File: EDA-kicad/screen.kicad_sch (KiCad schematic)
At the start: 3 parts

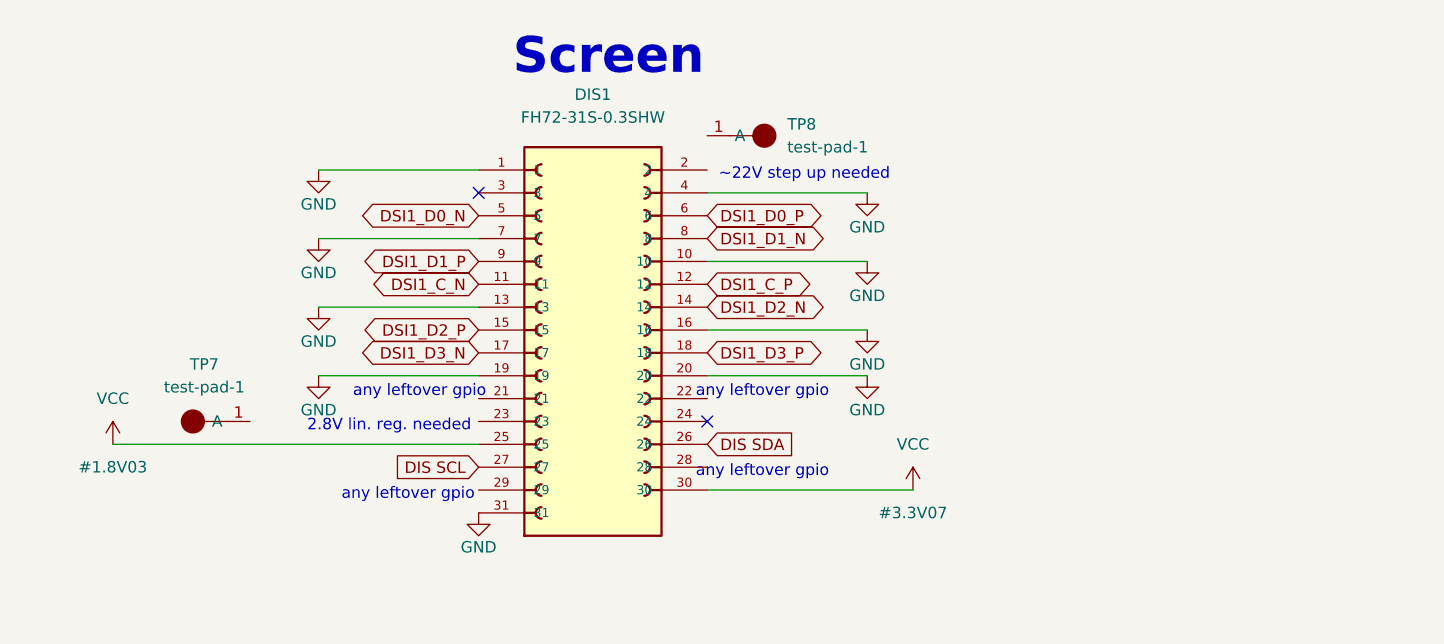
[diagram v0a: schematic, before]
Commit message: schematic cleaned up a bit
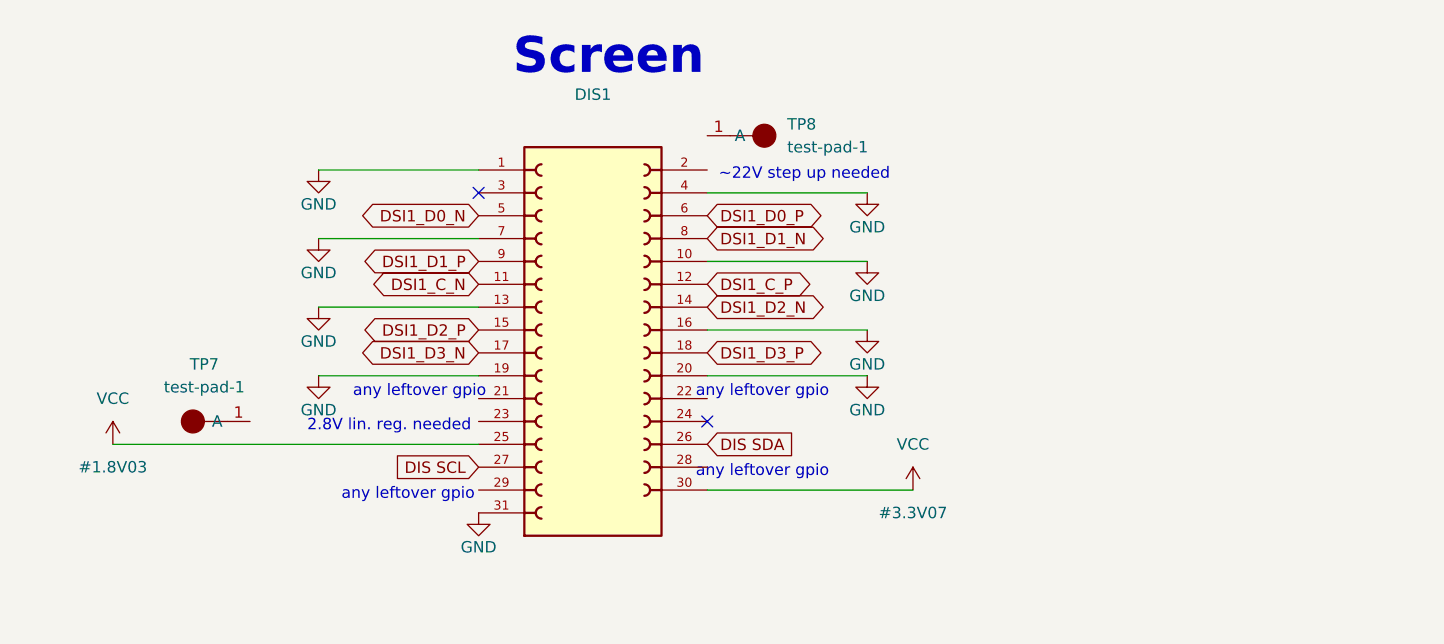
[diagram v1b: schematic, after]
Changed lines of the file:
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@@
 					(size 1.27 1.27)
 				)
+				(hide yes)
 			)
 		)
@@
 			)
 		)
-		(property "Description" "\n31 Position FPC Connector Contacts, Top 0.012 (0.30mm) Surface Mount, Right Angle\n"
+		(property "Description" "31 Position FPC Connector Contacts, Top 0.012 (0.30mm) Surface Mount, Right Angle"
 			(at 149.86 90.17 0)
 			(effects

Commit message: reannotate entire schematic
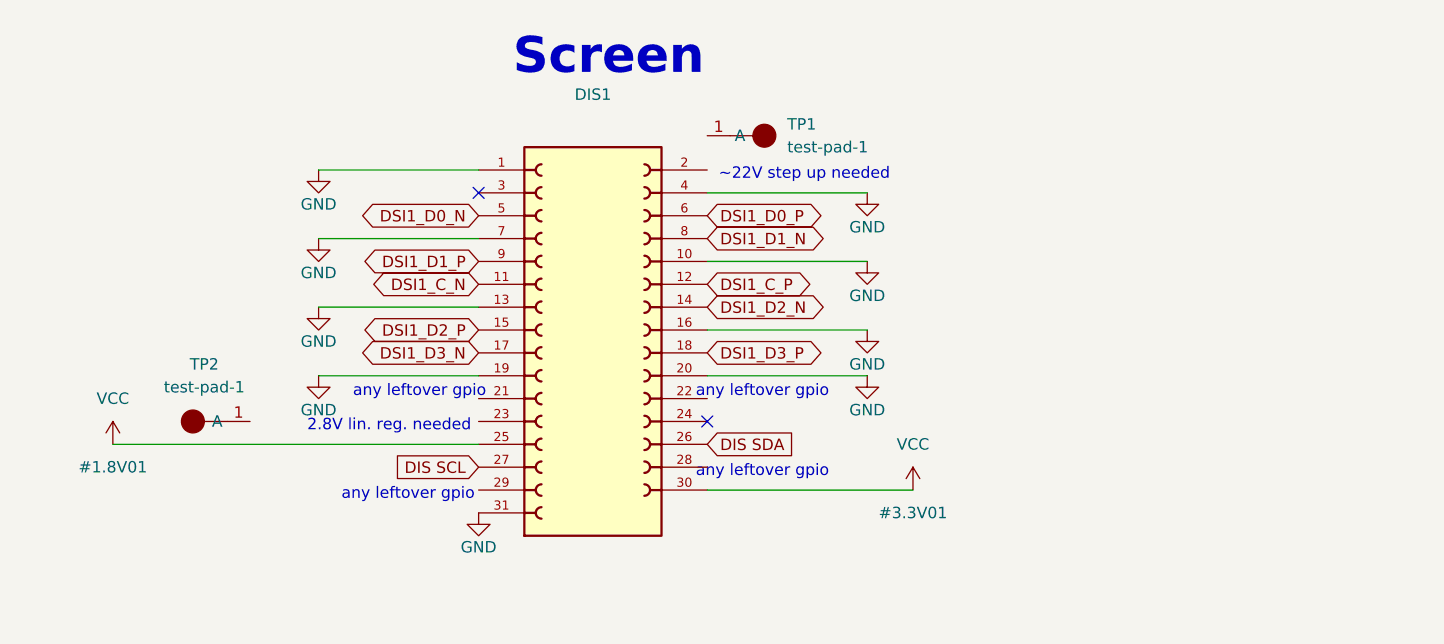
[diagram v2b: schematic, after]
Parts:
- renumbered TP8 to TP1, TP7 to TP2
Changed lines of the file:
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@@
 		(dnp no)
 		(fields_autoplaced yes)
-		(property "Reference" "TP7"
+		(property "Reference" "TP2"
 			(at 106.68 93.98 0)
 			(effects
@@
 			(project "cm5-carrier"
 				(path "/28c5e4fe-1ec7-4477-97f0-d2ec1401fad5/02797719-74e3-4dee-b809-c2968ee0cdff"
-					(reference "TP7")
+					(reference "TP2")
 					(unit 1)
 				)
@@
 		(on_board yes)
 		(dnp no)
-		(property "Reference" "#PWR070"
+		(property "Reference" "#PWR060"
 			(at 119.38 101.6 0)
 			(effects
@@
 			(project "cm5-carrier"
 				(path "/28c5e4fe-1ec7-4477-97f0-d2ec1401fad5/02797719-74e3-4dee-b809-c2968ee0cdff"
-					(reference "#PWR070")
+					(reference "#PWR060")
 					(unit 1)
 				)
@@
 		(on_board yes)
 		(dnp no)
-		(property "Reference" "#PWR067"
+		(property "Reference" "#PWR054"
 			(at 119.38 78.74 0)
 			(effects
@@
 			(project "cm5-carrier"
 				(path "/28c5e4fe-1ec7-4477-97f0-d2ec1401fad5/02797719-74e3-4dee-b809-c2968ee0cdff"
-					(reference "#PWR067")
+					(reference "#PWR054")
 					(unit 1)
 				)
@@
 		(on_board yes)
 		(dnp no)
-		(property "Reference" "#PWR074"
+		(property "Reference" "#PWR059"
 			(at 180.34 96.52 0)
 			(effects
@@
 			(project "cm5-carrier"
 				(path "/28c5e4fe-1ec7-4477-97f0-d2ec1401fad5/02797719-74e3-4dee-b809-c2968ee0cdff"
-					(reference "#PWR074")
+					(reference "#PWR059")
 					(unit 1)
 				)
@@
 		(on_board yes)
 		(dnp no)
-		(property "Reference" "#PWR075"
+		(property "Reference" "#PWR061"
 			(at 180.34 101.6 0)
 			(effects
@@
 			(project "cm5-carrier"
 				(path "/28c5e4fe-1ec7-4477-97f0-d2ec1401fad5/02797719-74e3-4dee-b809-c2968ee0cdff"
-					(reference "#PWR075")
+					(reference "#PWR061")
 					(unit 1)
 				)
@@
 		(on_board yes)
 		(dnp no)
-		(property "Reference" "#3.3V07"
+		(property "Reference" "#3.3V01"
 			(at 185.42 110.49 0)
 			(effects
@@
 			(project "cm5-carrier"
 				(path "/28c5e4fe-1ec7-4477-97f0-d2ec1401fad5/02797719-74e3-4dee-b809-c2968ee0cdff"
-					(reference "#3.3V07")
+					(reference "#3.3V01")
 					(unit 1)
 				)
@@
 		(dnp no)
 		(fields_autoplaced yes)
-		(property "Reference" "TP8"
+		(property "Reference" "TP1"
 			(at 171.45 67.3099 0)
 			(effects
@@
 			(project "cm5-carrier"
 				(path "/28c5e4fe-1ec7-4477-97f0-d2ec1401fad5/02797719-74e3-4dee-b809-c2968ee0cdff"
-					(reference "TP8")
+					(reference "TP1")
 					(unit 1)
 				)
@@
 		(on_board yes)
 		(dnp no)
-		(property "Reference" "#PWR069"
+		(property "Reference" "#PWR058"
 			(at 119.38 93.98 0)
 			(effects
@@
 			(project "cm5-carrier"
 				(path "/28c5e4fe-1ec7-4477-97f0-d2ec1401fad5/02797719-74e3-4dee-b809-c2968ee0cdff"
-					(reference "#PWR069")
+					(reference "#PWR058")
 					(unit 1)
 				)
@@
 		(on_board yes)
 		(dnp no)
-		(property "Reference" "#PWR071"
+		(property "Reference" "#PWR062"
 			(at 137.16 116.84 0)
 			(effects
@@
 			(project "cm5-carrier"
 				(path "/28c5e4fe-1ec7-4477-97f0-d2ec1401fad5/02797719-74e3-4dee-b809-c2968ee0cdff"
-					(reference "#PWR071")
+					(reference "#PWR062")
 					(unit 1)
 				)
@@
 		(on_board yes)
 		(dnp no)
-		(property "Reference" "#PWR068"
+		(property "Reference" "#PWR056"
 			(at 119.38 86.36 0)
 			(effects
@@
 			(project "cm5-carrier"
 				(path "/28c5e4fe-1ec7-4477-97f0-d2ec1401fad5/02797719-74e3-4dee-b809-c2968ee0cdff"
-					(reference "#PWR068")
+					(reference "#PWR056")
 					(unit 1)
 				)
@@
 		(on_board yes)
 		(dnp no)
-		(property "Reference" "#1.8V03"
+		(property "Reference" "#1.8V01"
 			(at 96.52 105.41 0)
 			(effects
@@
 			(project "cm5-carrier"
 				(path "/28c5e4fe-1ec7-4477-97f0-d2ec1401fad5/02797719-74e3-4dee-b809-c2968ee0cdff"
-					(reference "#1.8V03")
+					(reference "#1.8V01")
 					(unit 1)
 				)
@@
 		(on_board yes)
 		(dnp no)
-		(property "Reference" "#PWR072"
+		(property "Reference" "#PWR055"
 			(at 180.34 81.28 0)
 			(effects
@@
 			(project "cm5-carrier"
 				(path "/28c5e4fe-1ec7-4477-97f0-d2ec1401fad5/02797719-74e3-4dee-b809-c2968ee0cdff"
-					(reference "#PWR072")
+					(reference "#PWR055")
 					(unit 1)
 				)
@@
 		(on_board yes)
 		(dnp no)
-		(property "Reference" "#PWR073"
+		(property "Reference" "#PWR057"
 			(at 180.34 88.9 0)
 			(effects
@@
 			(project "cm5-carrier"
 				(path "/28c5e4fe-1ec7-4477-97f0-d2ec1401fad5/02797719-74e3-4dee-b809-c2968ee0cdff"
-					(reference "#PWR073")
-					(unit 1)
-				)
+					(reference "#PWR057")
+					(unit 1)
+				)

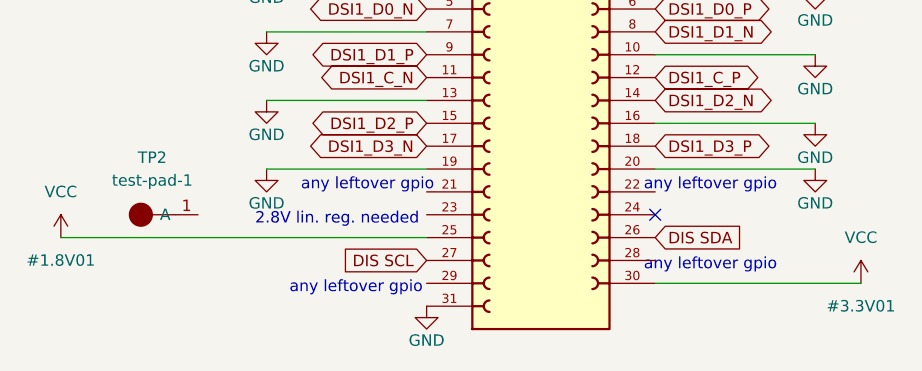
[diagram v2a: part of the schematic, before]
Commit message: add new switches and reannotate
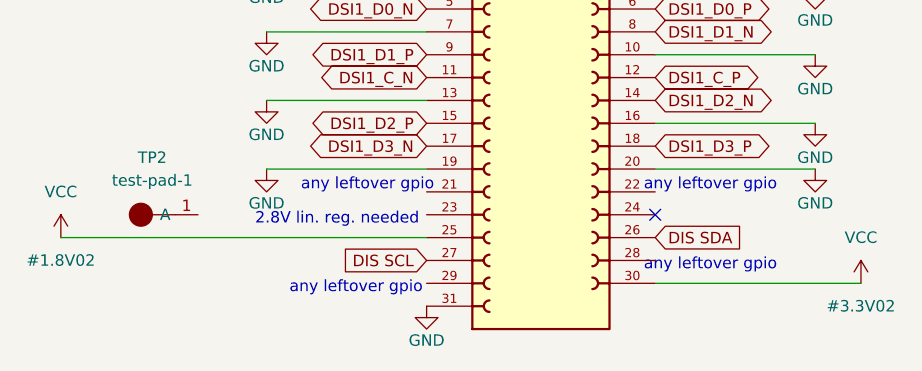
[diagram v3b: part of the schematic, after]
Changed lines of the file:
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@@
 		(on_board yes)
 		(dnp no)
-		(property "Reference" "#3.3V01"
+		(property "Reference" "#3.3V02"
 			(at 185.42 110.49 0)
 			(effects
@@
 			(project "cm5-carrier"
 				(path "/28c5e4fe-1ec7-4477-97f0-d2ec1401fad5/02797719-74e3-4dee-b809-c2968ee0cdff"
-					(reference "#3.3V01")
+					(reference "#3.3V02")
 					(unit 1)
 				)
@@
 		(on_board yes)
 		(dnp no)
-		(property "Reference" "#1.8V01"
+		(property "Reference" "#1.8V02"
 			(at 96.52 105.41 0)
 			(effects
@@
 			(project "cm5-carrier"
 				(path "/28c5e4fe-1ec7-4477-97f0-d2ec1401fad5/02797719-74e3-4dee-b809-c2968ee0cdff"
-					(reference "#1.8V01")
-					(unit 1)
-				)
+					(reference "#1.8V02")
+					(unit 1)
+				)

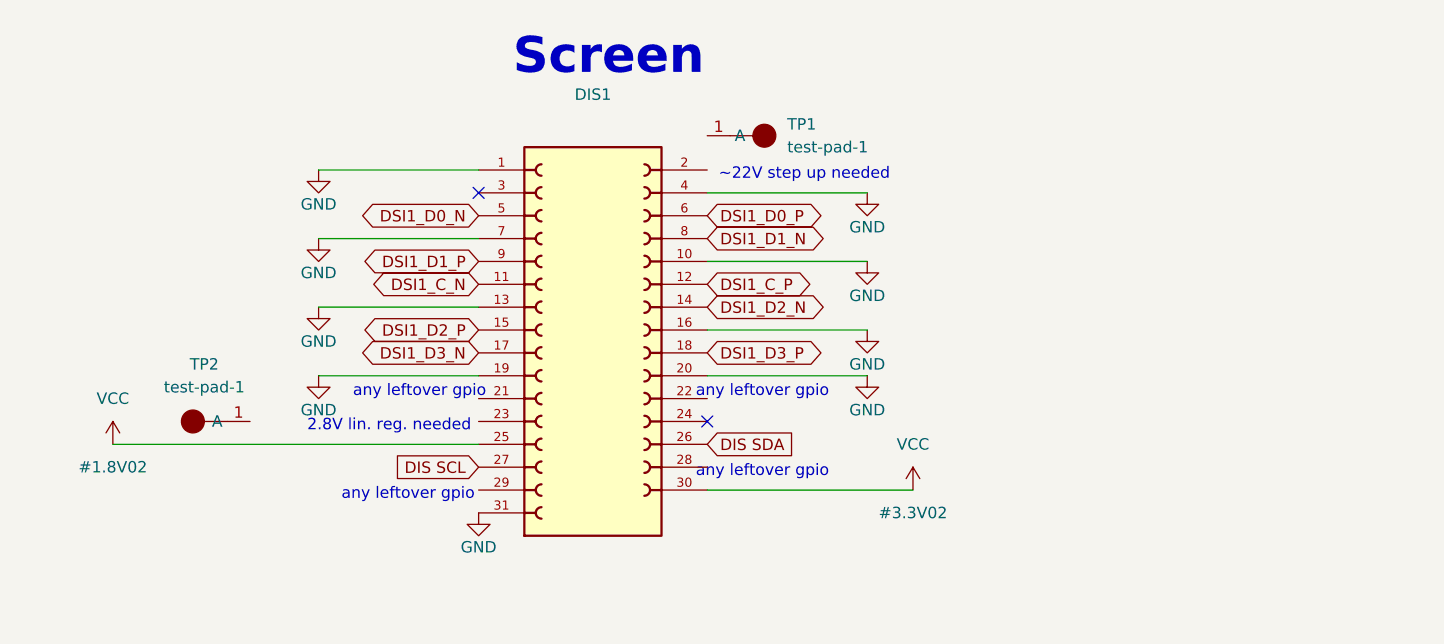
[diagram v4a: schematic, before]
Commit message: set everything except from power to DNP
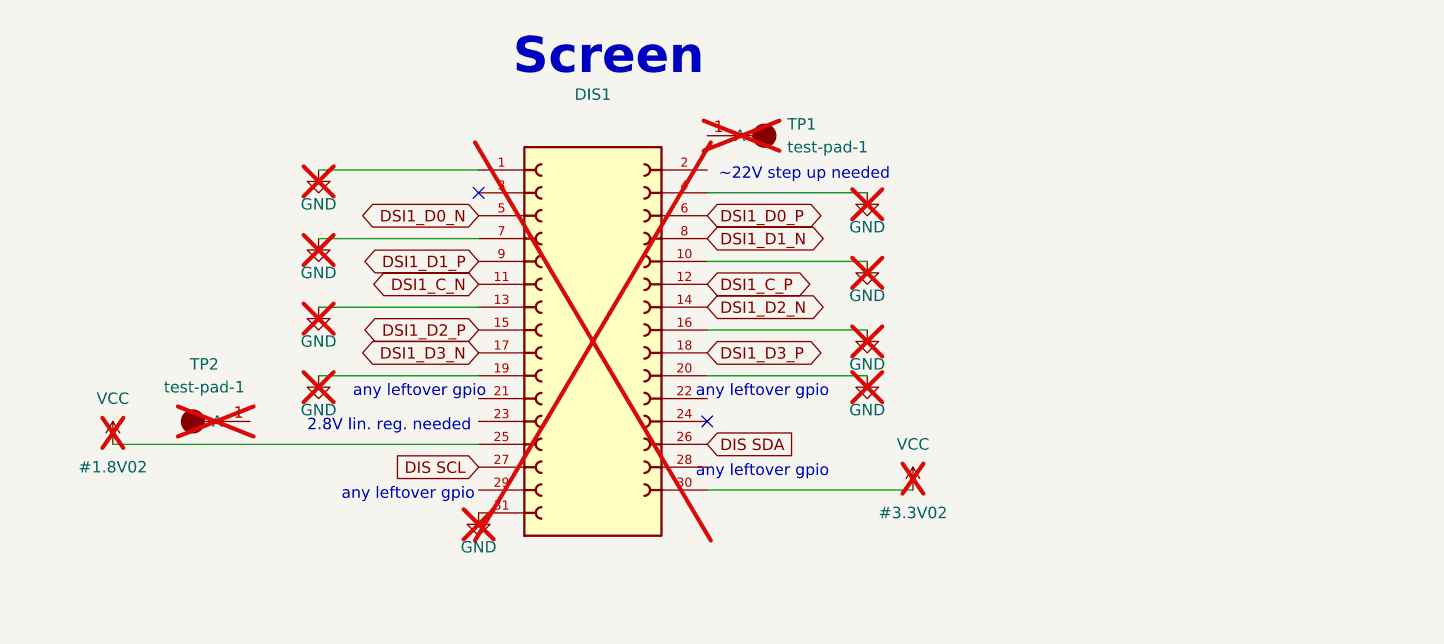
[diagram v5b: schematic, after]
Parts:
- DIS1, TP1, TP2: now not fitted

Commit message: setup layers
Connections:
- net 22V: now reaches DIS1.2
- net VCC renamed 1V8
- net 1V8: no longer DIS1.30
- new net 3V3B: DIS1.30
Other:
- note added: "https://www.nxp.com/docs/en/supporting-information/RK055AHD091-CTG.pdf"
- note removed: "~22V step up needed"

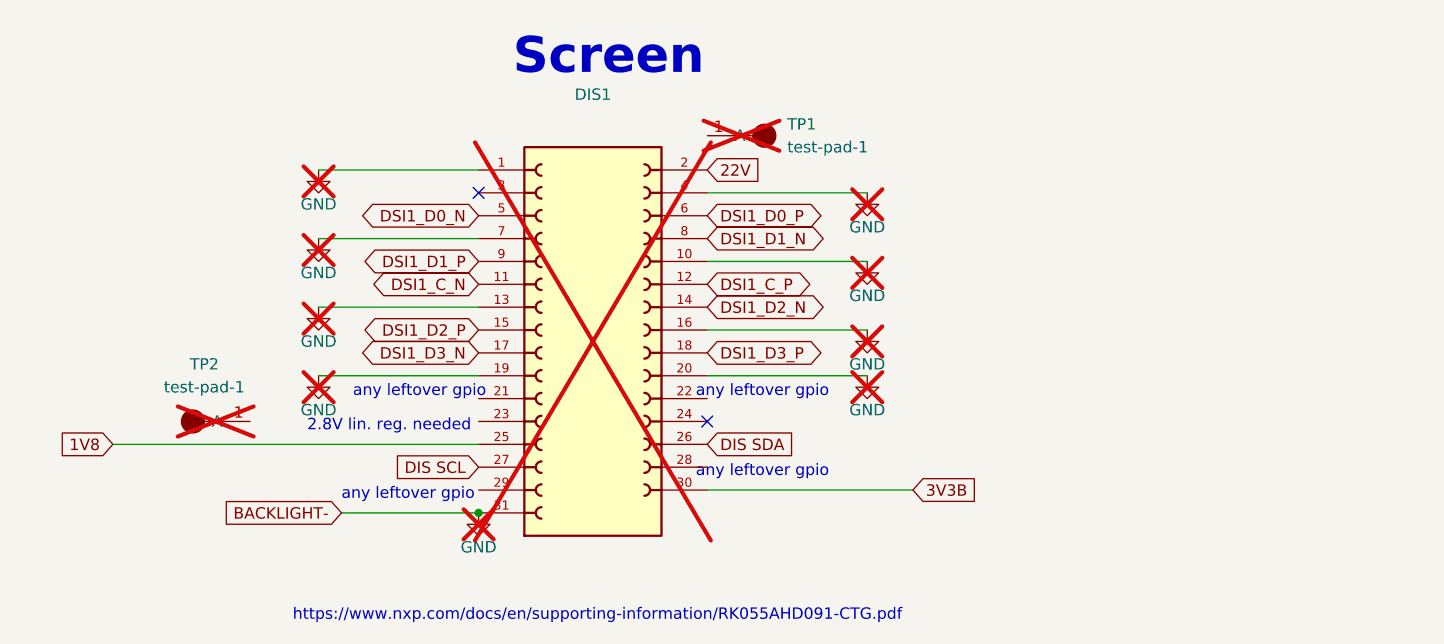
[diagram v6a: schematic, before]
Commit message: Improve KiCAD schematic design and labeling
- Replace overused global labels with hierarchical and local labels
- Add proper GND connections to components
- Fix BACKLIGHT- net issues
- Apply minor schematic fixes and cleanups
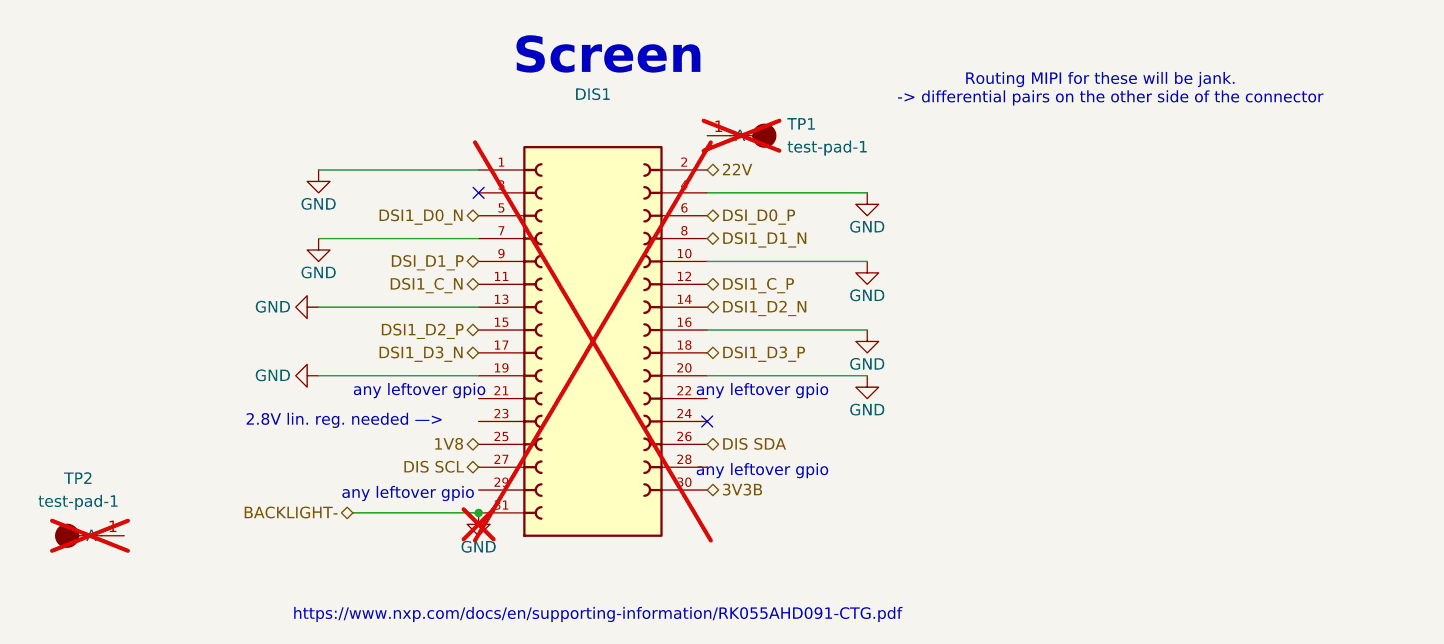
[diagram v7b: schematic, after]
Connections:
- net DSI1_D0_P renamed DSI_D0_P
- net DSI1_D1_P renamed DSI_D1_P
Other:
- note added: "2.8V lin. reg. needed —>"
- note added: "Routing MIPI for these will be jank. -> differential pairs on the other side of the connector"
- note removed: "2.8V lin. reg. needed"
- moved on the sheet: TP2
